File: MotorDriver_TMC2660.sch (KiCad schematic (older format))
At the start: 16 parts, among them U4 TMC2660

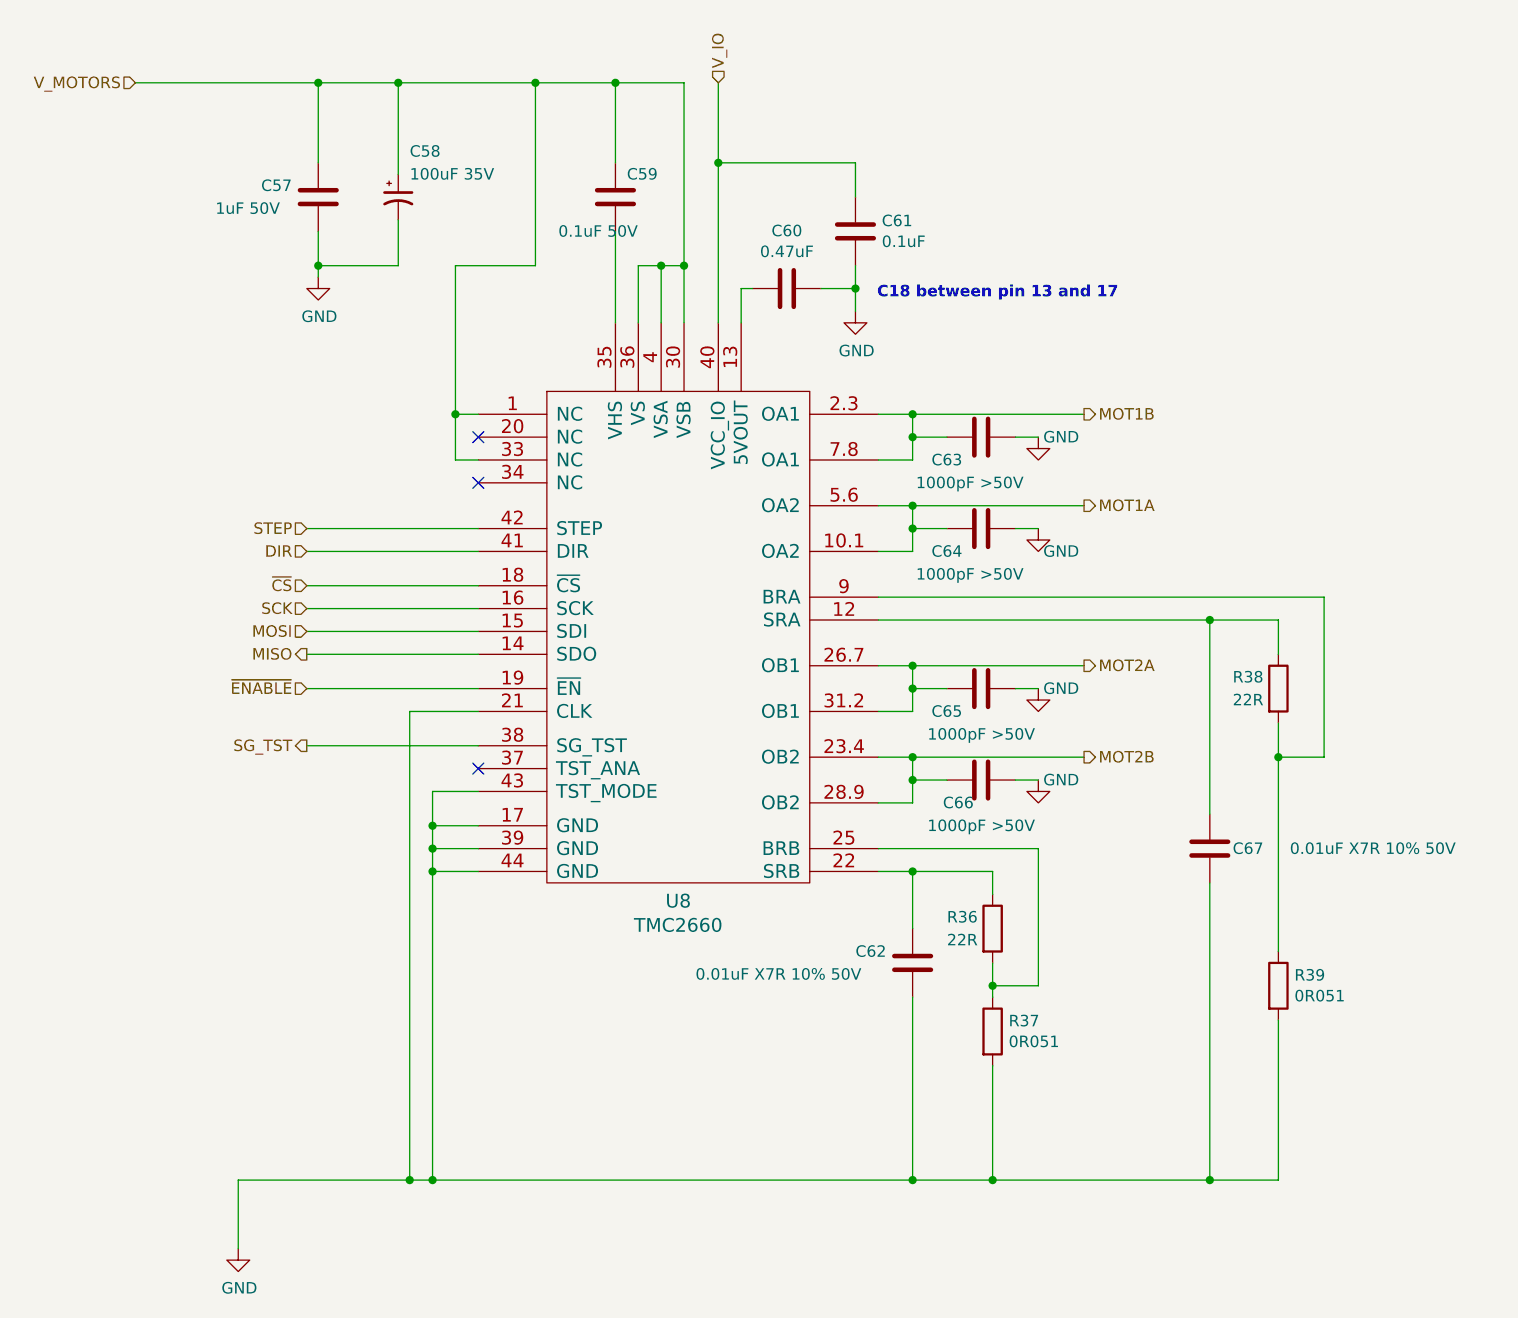
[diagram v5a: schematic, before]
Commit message: Updated components. Removed power supply. Component layout on PCB.
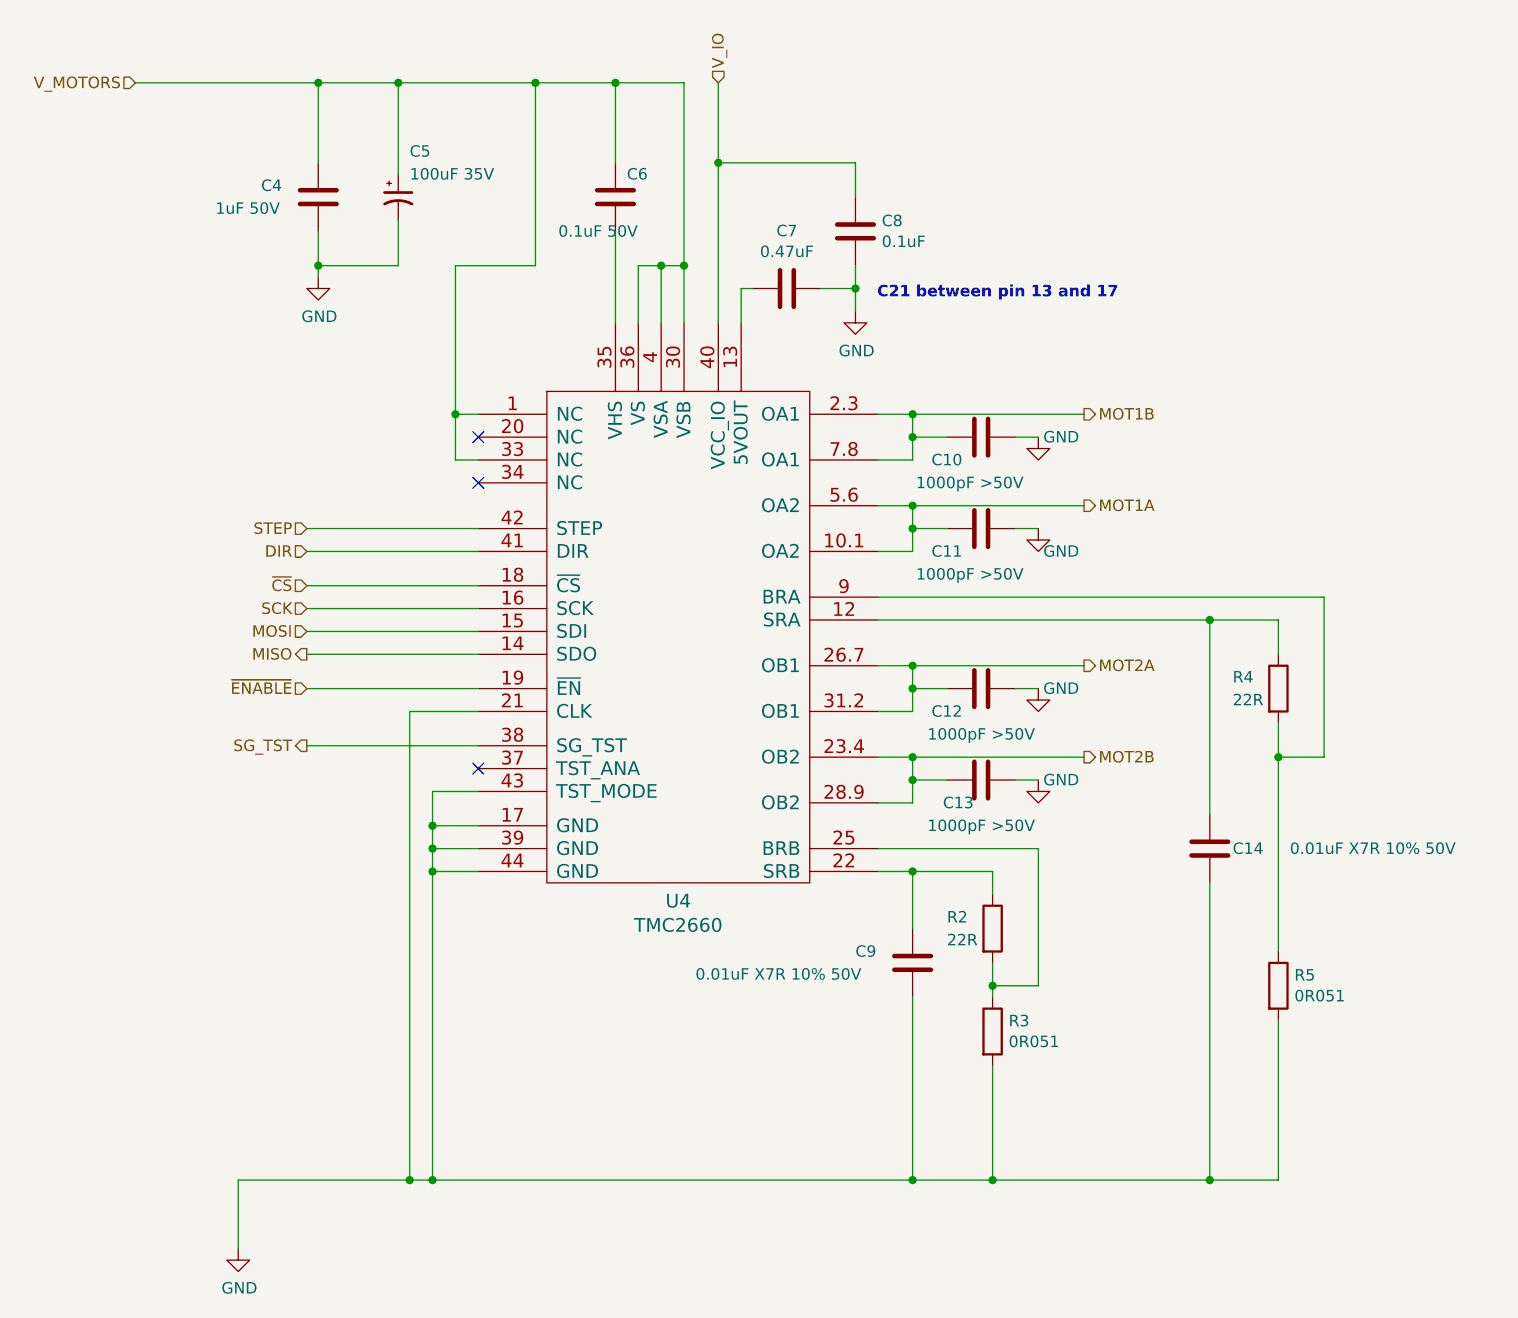
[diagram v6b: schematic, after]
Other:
- note added: "C21 between pin 13 and 17"
- note removed: "C18 between pin 13 and 17"
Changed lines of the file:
@@
 $Descr A4 11693 8268
 encoding utf-8
-Sheet 26 35
+Sheet 9 34
 Title ""
 Date ""
@@
 AR Path="/5AC337B6/5ACE1C6D/5ACC0B66/5AC338BF" Ref="U7"  Part="1"
 AR Path="/5AC337B6/5AD9F95A/5AD4B0F5/5AC338BF" Ref="U8"  Part="1"
-F 0 "U8" H 4875 2520 60  0000 C CNN
+F 0 "U4" H 4875 2520 60  0000 C CNN
 F 1 "TMC2660" H 4875 2414 60  0000 C CNN
 F 2 "PrntrBoardV1:TMC2660" H 4900 3600 60  0001 C CNN
@@
 AR Path="/5AC337B6/5ACE1C6D/5ACC0B66/5AC33A94" Ref="C46"  Part="1"
 AR Path="/5AC337B6/5AD9F95A/5AD4B0F5/5AC33A94" Ref="C59"  Part="1"
-F 0 "C59" H 4650 1800 50  0000 L CNN
+F 0 "C6" H 4650 1800 50  0000 L CNN
 F 1 "0.1uF 50V" H 4350 1550 50  0000 L CNN
 F 2 "Capacitor_SMD:C_0603_1608Metric" H 4638 1550 50  0001 C CNN
@@
 AR Path="/5AC337B6/5ACE1C6D/5ACC0B66/5AC33B3C" Ref="C44"  Part="1"
 AR Path="/5AC337B6/5AD9F95A/5AD4B0F5/5AC33B3C" Ref="C57"  Part="1"
-F 0 "C57" H 3050 1750 50  0000 L CNN
+F 0 "C4" H 3050 1750 50  0000 L CNN
 F 1 "1uF 50V" H 2850 1650 50  0000 L CNN
 F 2 "Capacitor_SMD:C_0603_1608Metric" H 3338 1550 50  0001 C CNN
@@
 AR Path="/5AC337B6/5ACE1C6D/5ACC0B66/5AC33B85" Ref="C47"  Part="1"
 AR Path="/5AC337B6/5AD9F95A/5AD4B0F5/5AC33B85" Ref="C60"  Part="1"
-F 0 "C60" V 5098 2100 50  0000 C CNN
+F 0 "C7" V 5098 2100 50  0000 C CNN
 F 1 "0.47uF" V 5189 2100 50  0000 C CNN
 F 2 "Capacitor_SMD:C_0603_1608Metric" H 5388 1950 50  0001 C CNN
@@
 AR Path="/5AC337B6/5ACE1C6D/5ACC0B66/5AC33C56" Ref="C48"  Part="1"
 AR Path="/5AC337B6/5AD9F95A/5AD4B0F5/5AC33C56" Ref="C61"  Part="1"
-F 0 "C61" H 5765 1896 50  0000 L CNN
+F 0 "C8" H 5765 1896 50  0000 L CNN
 F 1 "0.1uF" H 5765 1805 50  0000 L CNN
 F 2 "Capacitor_SMD:C_0603_1608Metric" H 5688 1700 50  0001 C CNN
@@
 AR Path="/5AC337B6/5ACE1C6D/5ACC0B66/5AC33CA1" Ref="C50"  Part="1"
 AR Path="/5AC337B6/5AD9F95A/5AD4B0F5/5AC33CA1" Ref="C63"  Part="1"
-F 0 "C63" V 6300 2600 50  0000 C CNN
+F 0 "C10" V 6300 2600 50  0000 C CNN
 F 1 "1000pF >50V" V 6400 2700 50  0000 C CNN
 F 2 "Capacitor_SMD:C_0603_1608Metric" H 6238 2600 50  0001 C CNN
@@
 AR Path="/5AC337B6/5ACE1C6D/5ACC0B66/5AC33D6E" Ref="C51"  Part="1"
 AR Path="/5AC337B6/5AD9F95A/5AD4B0F5/5AC33D6E" Ref="C64"  Part="1"
-F 0 "C64" V 6300 3000 50  0000 C CNN
+F 0 "C11" V 6300 3000 50  0000 C CNN
 F 1 "1000pF >50V" V 6400 3100 50  0000 C CNN
 F 2 "Capacitor_SMD:C_0603_1608Metric" H 6238 3000 50  0001 C CNN
@@
 AR Path="/5AC337B6/5ACE1C6D/5ACC0B66/5AC33DC1" Ref="C52"  Part="1"
 AR Path="/5AC337B6/5AD9F95A/5AD4B0F5/5AC33DC1" Ref="C65"  Part="1"
-F 0 "C65" V 6300 3700 50  0000 C CNN
+F 0 "C12" V 6300 3700 50  0000 C CNN
 F 1 "1000pF >50V" V 6400 3850 50  0000 C CNN
 F 2 "Capacitor_SMD:C_0603_1608Metric" H 6238 3700 50  0001 C CNN
@@
 AR Path="/5AC337B6/5ACE1C6D/5ACC0B66/5AC33E6E" Ref="C53"  Part="1"
 AR Path="/5AC337B6/5AD9F95A/5AD4B0F5/5AC33E6E" Ref="C66"  Part="1"
-F 0 "C66" V 6300 4150 50  0000 C CNN
+F 0 "C13" V 6300 4150 50  0000 C CNN
 F 1 "1000pF >50V" V 6400 4250 50  0000 C CNN
 F 2 "Capacitor_SMD:C_0603_1608Metric" H 6238 4100 50  0001 C CNN
@@
 AR Path="/5AC337B6/5ACE1C6D/5ACC0B66/5AC33EDF" Ref="C54"  Part="1"
 AR Path="/5AC337B6/5AD9F95A/5AD4B0F5/5AC33EDF" Ref="C67"  Part="1"
-F 0 "C67" H 7300 4550 50  0000 L CNN
+F 0 "C14" H 7300 4550 50  0000 L CNN
 F 1 "0.01uF X7R 10% 50V" H 7550 4550 50  0000 L CNN
 F 2 "Capacitor_SMD:C_0603_1608Metric" H 7238 4400 50  0001 C CNN
@@
 AR Path="/5AC337B6/5ACE1C6D/5ACC0B66/5AC33F7D" Ref="C49"  Part="1"
 AR Path="/5AC337B6/5AD9F95A/5AD4B0F5/5AC33F7D" Ref="C62"  Part="1"
-F 0 "C62" H 5650 5100 50  0000 L CNN
+F 0 "C9" H 5650 5100 50  0000 L CNN
 F 1 "0.01uF X7R 10% 50V" H 4950 5000 50  0000 L CNN
 F 2 "Capacitor_SMD:C_0603_1608Metric" H 5938 4900 50  0001 C CNN
@@
 AR Path="/5AC337B6/5ACE1C6D/5ACC0B66/5AC34593" Ref="#PWR049"  Part="1"
 AR Path="/5AC337B6/5AD9F95A/5AD4B0F5/5AC34593" Ref="#PWR059"  Part="1"
-F 0 "#PWR059" H 5650 1950 50  0001 C CNN
+F 0 "#PWR014" H 5650 1950 50  0001 C CNN
 F 1 "GND" H 5655 2027 50  0000 C CNN
 F 2 "" H 5650 2200 50  0001 C CNN
@@
 AR Path="/5AC337B6/5ACE1C6D/5ACC0B66/5AC345D6" Ref="#PWR048"  Part="1"
 AR Path="/5AC337B6/5AD9F95A/5AD4B0F5/5AC345D6" Ref="#PWR058"  Part="1"
-F 0 "#PWR058" H 3300 1800 50  0001 C CNN
+F 0 "#PWR013" H 3300 1800 50  0001 C CNN
 F 1 "GND" H 3305 1877 50  0000 C CNN
 F 2 "" H 3300 2050 50  0001 C CNN
@@
 AR Path="/5AC337B6/5ACE1C6D/5ACC0B66/5AC34619" Ref="#PWR050"  Part="1"
 AR Path="/5AC337B6/5AD9F95A/5AD4B0F5/5AC34619" Ref="#PWR060"  Part="1"
-F 0 "#PWR060" H 6450 2500 50  0001 C CNN
+F 0 "#PWR015" H 6450 2500 50  0001 C CNN
 F 1 "GND" H 6550 2750 50  0000 C CNN
 F 2 "" H 6450 2750 50  0001 C CNN
@@
 AR Path="/5AC337B6/5ACE1C6D/5ACC0B66/5AC3465C" Ref="#PWR051"  Part="1"
 AR Path="/5AC337B6/5AD9F95A/5AD4B0F5/5AC3465C" Ref="#PWR061"  Part="1"
-F 0 "#PWR061" H 6450 2900 50  0001 C CNN
+F 0 "#PWR016" H 6450 2900 50  0001 C CNN
 F 1 "GND" H 6550 3050 50  0000 C CNN
 F 2 "" H 6450 3150 50  0001 C CNN
@@
 AR Path="/5AC337B6/5ACE1C6D/5ACC0B66/5AC3469F" Ref="#PWR052"  Part="1"
 AR Path="/5AC337B6/5AD9F95A/5AD4B0F5/5AC3469F" Ref="#PWR062"  Part="1"
-F 0 "#PWR062" H 6450 3600 50  0001 C CNN
+F 0 "#PWR017" H 6450 3600 50  0001 C CNN
 F 1 "GND" H 6550 3850 50  0000 C CNN
 F 2 "" H 6450 3850 50  0001 C CNN
@@
 AR Path="/5AC337B6/5ACE1C6D/5ACC0B66/5AC346E2" Ref="#PWR053"  Part="1"
 AR Path="/5AC337B6/5AD9F95A/5AD4B0F5/5AC346E2" Ref="#PWR063"  Part="1"
-F 0 "#PWR063" H 6450 4000 50  0001 C CNN
+F 0 "#PWR018" H 6450 4000 50  0001 C CNN
 F 1 "GND" H 6550 4250 50  0000 C CNN
 F 2 "" H 6450 4250 50  0001 C CNN
@@
 AR Path="/5AC337B6/5ACE1C6D/5ACC0B66/5AC34725" Ref="#PWR047"  Part="1"
 AR Path="/5AC337B6/5AD9F95A/5AD4B0F5/5AC34725" Ref="#PWR057"  Part="1"
-F 0 "#PWR057" H 2950 6050 50  0001 C CNN
+F 0 "#PWR012" H 2950 6050 50  0001 C CNN
 F 1 "GND" H 2955 6127 50  0000 C CNN
 F 2 "" H 2950 6300 50  0001 C CNN
@@
 AR Path="/5AC337B6/5ACE1C6D/5ACC0B66/5AC3912E" Ref="R28"  Part="1"
 AR Path="/5AC337B6/5AD9F95A/5AD4B0F5/5AC3912E" Ref="R36"  Part="1"
-F 0 "R36" H 6050 4950 50  0000 L CNN
+F 0 "R2" H 6050 4950 50  0000 L CNN
 F 1 "22R" H 6050 4850 50  0000 L CNN
 F 2 "Resistor_SMD:R_0603_1608Metric" V 6180 4900 50  0001 C CNN
@@
 AR Path="/5AC337B6/5ACE1C6D/5ACC0B66/5AC391BE" Ref="R29"  Part="1"
 AR Path="/5AC337B6/5AD9F95A/5AD4B0F5/5AC391BE" Ref="R37"  Part="1"
-F 0 "R37" H 6320 5396 50  0000 L CNN
+F 0 "R3" H 6320 5396 50  0000 L CNN
 F 1 "0R051" H 6320 5305 50  0000 L CNN
 F 2 "Resistor_SMD:R_1206_3216Metric" V 6180 5350 50  0001 C CNN
@@
 AR Path="/5AC337B6/5ACE1C6D/5ACC0B66/5AC3921D" Ref="R30"  Part="1"
 AR Path="/5AC337B6/5AD9F95A/5AD4B0F5/5AC3921D" Ref="R38"  Part="1"
-F 0 "R38" H 7300 3900 50  0000 L CNN
+F 0 "R4" H 7300 3900 50  0000 L CNN
 F 1 "22R" H 7300 3800 50  0000 L CNN
 F 2 "Resistor_SMD:R_0603_1608Metric" V 7430 3850 50  0001 C CNN
@@
 AR Path="/5AC337B6/5ACE1C6D/5ACC0B66/5AC392A1" Ref="R31"  Part="1"
 AR Path="/5AC337B6/5AD9F95A/5AD4B0F5/5AC392A1" Ref="R39"  Part="1"
-F 0 "R39" H 7570 5196 50  0000 L CNN
+F 0 "R5" H 7570 5196 50  0000 L CNN
 F 1 "0R051" H 7570 5105 50  0000 L CNN
 F 2 "Resistor_SMD:R_1206_3216Metric" V 7430 5150 50  0001 C CNN
@@
 AR Path="/5AC337B6/5ACE1C6D/5ACC0B66/5AC55FA7" Ref="C45"  Part="1"
 AR Path="/5AC337B6/5AD9F95A/5AD4B0F5/5AC55FA7" Ref="C58"  Part="1"
-F 0 "C58" H 3700 1900 50  0000 L CNN
+F 0 "C5" H 3700 1900 50  0000 L CNN
 F 1 "100uF 35V" H 3700 1800 50  0000 L CNN
 F 2 "Capacitor_SMD:CP_Elec_6.3x7.7" H 3650 1700 50  0001 C CNN
@@
 	7200 6000 7500 6000
 Text Notes 6800 2150 2    50   ~ 10
-C18 between pin 13 and 17
+C21 between pin 13 and 17
 Text HLabel 3250 3150 0    50   Input ~ 0
 STEP
